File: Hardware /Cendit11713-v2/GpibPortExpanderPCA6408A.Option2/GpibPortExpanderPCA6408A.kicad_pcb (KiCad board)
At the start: 2 copper layers, 46 parts, among them P1 CONN_01X07, U1 PCA6408A, U2 PCA6408A

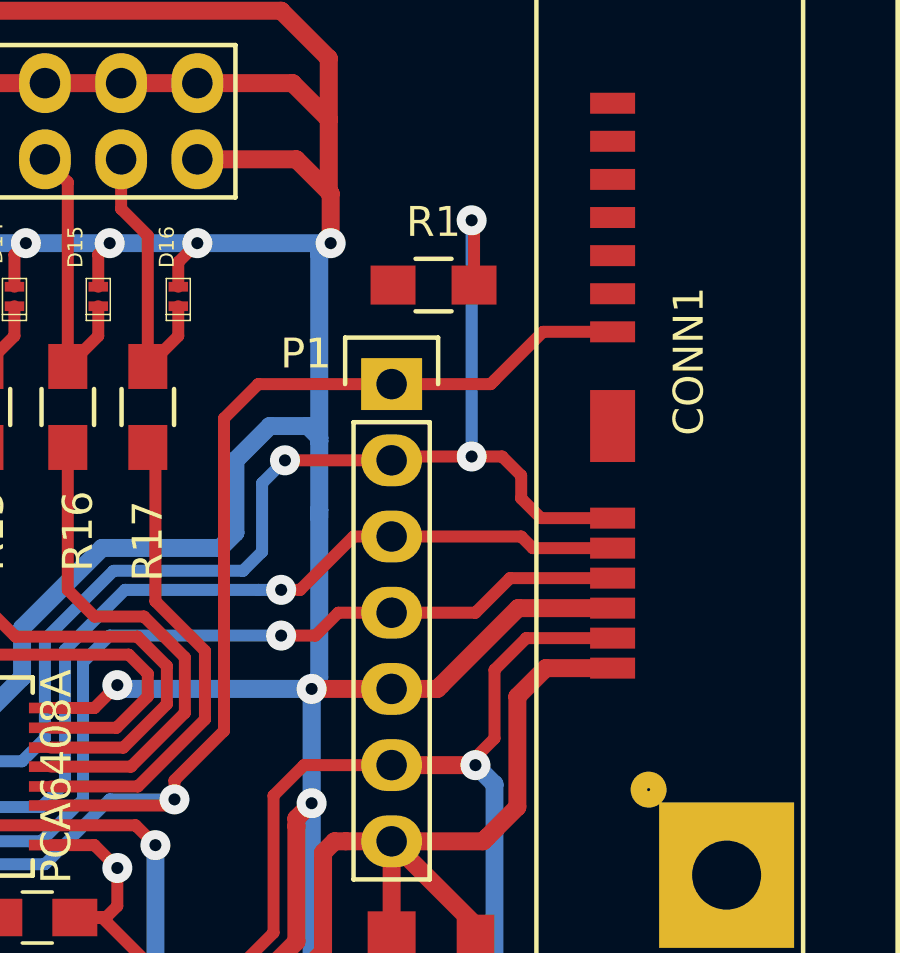
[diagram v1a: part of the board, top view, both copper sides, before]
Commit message: En Cendit11713 + CenditLab respaldo
  - Se revisan tarjetas
  - Correccion en PCB GPIB
  - Se inicia tarjeta madre en una pieza (MainBoard.OnePiece)
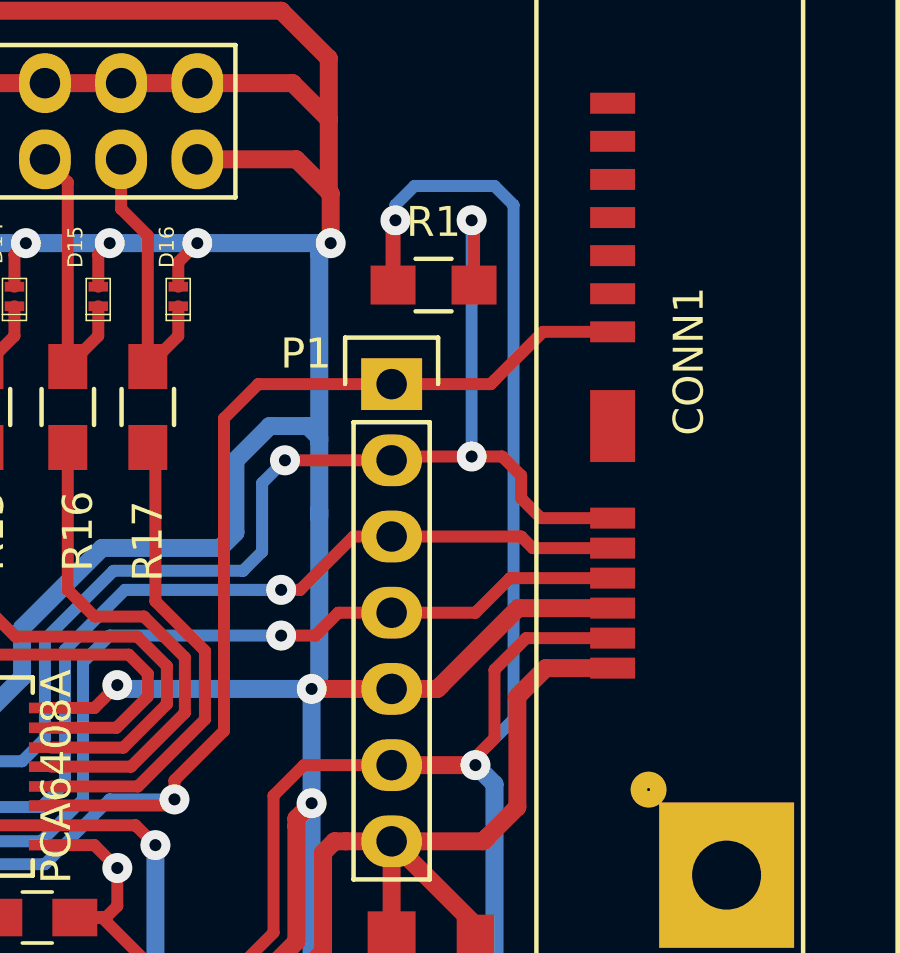
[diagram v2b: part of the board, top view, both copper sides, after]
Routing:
- net +3V3: track 74.0 -> 100.1 mm, vias 3 -> 4
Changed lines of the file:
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@@
   (general
     (links 113)
-    (no_connects 1)
-    (area 129.439999 71.019999 203.493572 137.320001)
+    (no_connects 0)
+    (area 0 0 0 0)
     (thickness 1.6)
     (drawings 6)
-    (tracks 606)
+    (tracks 615)
     (zones 0)
     (modules 46)
@@
   (page A4)
   (layers
-    (0 F.Cu signal)
+    (0 F.Cu signal hide)
     (31 B.Cu signal)
     (32 B.Adhes user)
@@
   )
   (setup
-    (last_trace_width 0.25)
+    (last_trace_width 0.4)
     (user_trace_width 0.3)
     (user_trace_width 0.325)
@@
       (padsonsilk false)
       (subtractmaskfromsilk false)
-      (outputformat 4)
+      (outputformat 1)
       (mirror false)
       (drillshape 0)
@@
   (segment (start 142.748 114.427) (end 143.129 114.427) (width 0.4) (layer F.Cu) (net 2))
   (segment (start 143.129 114.427) (end 144.419 114.427) (width 0.4) (layer F.Cu) (net 2))
+  (segment (start 175.133 109.347) (end 175.133 109.093) (width 0.5) (layer B.Cu) (net 3))
+  (segment (start 175.133 109.093) (end 176.403 107.823) (width 0.4) (layer B.Cu) (net 3))
+  (segment (start 172.386 91.266) (end 172.466 91.186) (width 0.5) (layer F.Cu) (net 3))
+  (via (at 172.466 91.186) (size 1) (drill 0.4) (layers F.Cu B.Cu) (net 3))
+  (segment (start 172.386 93.345) (end 172.386 91.266) (width 0.5) (layer F.Cu) (net 3) (status 400000))
+  (segment (start 172.466 90.678) (end 172.466 91.186) (width 0.4) (layer B.Cu) (net 3))
+  (segment (start 173.101 90.043) (end 172.466 90.678) (width 0.4) (layer B.Cu) (net 3))
+  (segment (start 175.768 90.043) (end 173.101 90.043) (width 0.4) (layer B.Cu) (net 3))
+  (segment (start 176.403 90.678) (end 175.768 90.043) (width 0.4) (layer B.Cu) (net 3))
+  (segment (start 176.403 107.823) (end 176.403 90.678) (width 0.4) (layer B.Cu) (net 3))
   (segment (start 180.372 118.618) (end 180.372 120.765) (width 0.6) (layer F.Cu) (net 3))
   (segment (start 180.372 120.765) (end 180.106 121.031) (width 0.4) (layer F.Cu) (net 3))
@@
   (segment (start 175.768 117.094) (end 177.292 118.618) (width 0.6) (layer B.Cu) (net 3))
   (segment (start 175.768 109.982) (end 175.768 117.094) (width 0.6) (layer B.Cu) (net 3))
-  (segment (start 175.133 109.347) (end 175.133 109.093) (width 0.4) (layer F.Cu) (net 3))
   (segment (start 175.768 108.458) (end 175.768 106.172) (width 0.4) (layer F.Cu) (net 3))
   (segment (start 176.826 105.114) (end 179.705 105.114) (width 0.4) (layer F.Cu) (net 3))
